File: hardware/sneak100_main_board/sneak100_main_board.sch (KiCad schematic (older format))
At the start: 0 parts

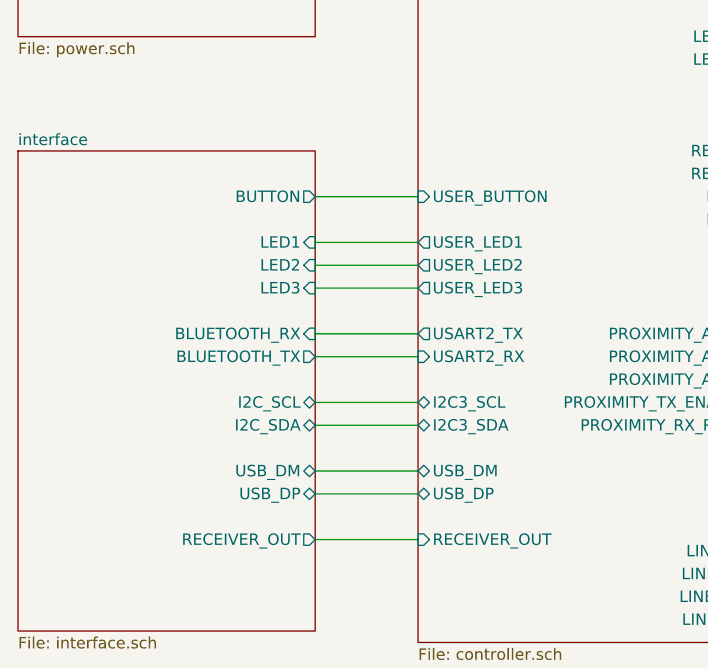
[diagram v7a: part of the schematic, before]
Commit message: delete USB, modify top hull, bigger PCB board
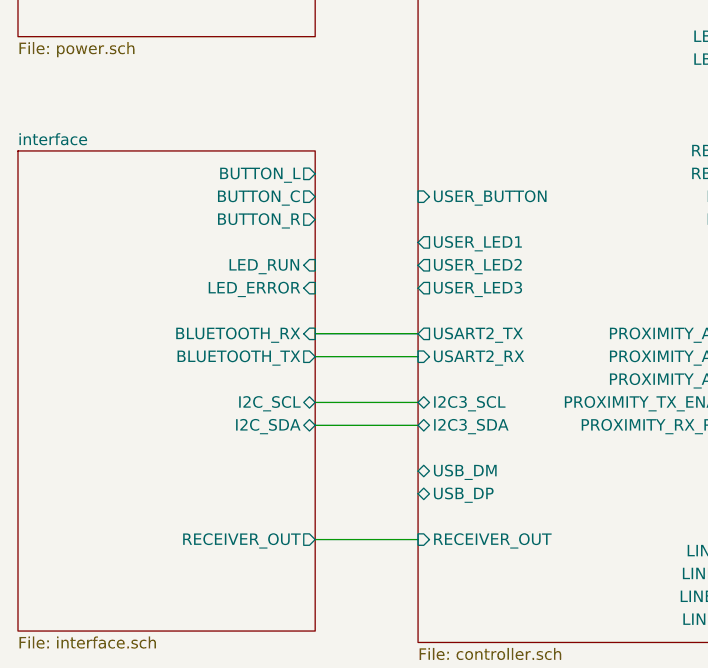
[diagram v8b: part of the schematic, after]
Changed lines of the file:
@@
 	6400 5550 6900 5550
-Wire Wire Line
-	4450 3700 4900 3700
-Wire Wire Line
-	4450 3900 4900 3900
-Wire Wire Line
-	4450 4000 4900 4000
-Wire Wire Line
-	4450 4100 4900 4100
-Wire Wire Line
-	4900 4900 4450 4900
-Wire Wire Line
-	4900 5000 4450 5000
 Wire Wire Line
 	4900 4300 4450 4300
@@
 Wire Wire Line
 	4450 2450 4900 2450
-$Sheet
-S 3150 3500 1300 2100
-U 60E0491A
-F0 "interface" 50
-F1 "interface.sch" 50
-F2 "LED1" I R 4450 3900 50
-F3 "LED2" I R 4450 4000 50
-F4 "LED3" I R 4450 4100 50
-F5 "USB_DP" B R 4450 5000 50
-F6 "USB_DM" B R 4450 4900 50
-F7 "BLUETOOTH_RX" I R 4450 4300 50
-F8 "BLUETOOTH_TX" O R 4450 4400 50
-F9 "I2C_SDA" B R 4450 4700 50
-F10 "I2C_SCL" B R 4450 4600 50
-F11 "RECEIVER_OUT" O R 4450 5200 50
-F12 "BUTTON" O R 4450 3700 50
-$EndSheet
 $Sheet
 S 4900 1900 1500 3750
@@
 F38 "RECEIVER_OUT" I L 4900 5200 50
 $EndSheet
+$Sheet
+S 3150 3500 1300 2100
+U 60E0491A
+F0 "interface" 50
+F1 "interface.sch" 50
+F2 "BLUETOOTH_RX" I R 4450 4300 50
+F3 "BLUETOOTH_TX" O R 4450 4400 50
+F4 "I2C_SDA" B R 4450 4700 50
+F5 "I2C_SCL" B R 4450 4600 50
+F6 "RECEIVER_OUT" O R 4450 5200 50
+F7 "BUTTON_L" O R 4450 3600 50
+F8 "LED_RUN" I R 4450 4000 50
+F9 "BUTTON_C" O R 4450 3700 50
+F10 "BUTTON_R" O R 4450 3800 50
+F11 "LED_ERROR" I R 4450 4100 50
+$EndSheet
 $EndSCHEMATC
